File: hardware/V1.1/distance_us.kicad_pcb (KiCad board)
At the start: 2 copper layers, 20 x 45 mm, 26 parts, among them P1 CON-SENSOR, P2 CONN_4, Q1 2N7002P, Q2 2N7002P, U1 LMV358LI, U2 M24C64, U3 DRILL, U4 DRILL, U5 DRILL, U6 DRILL

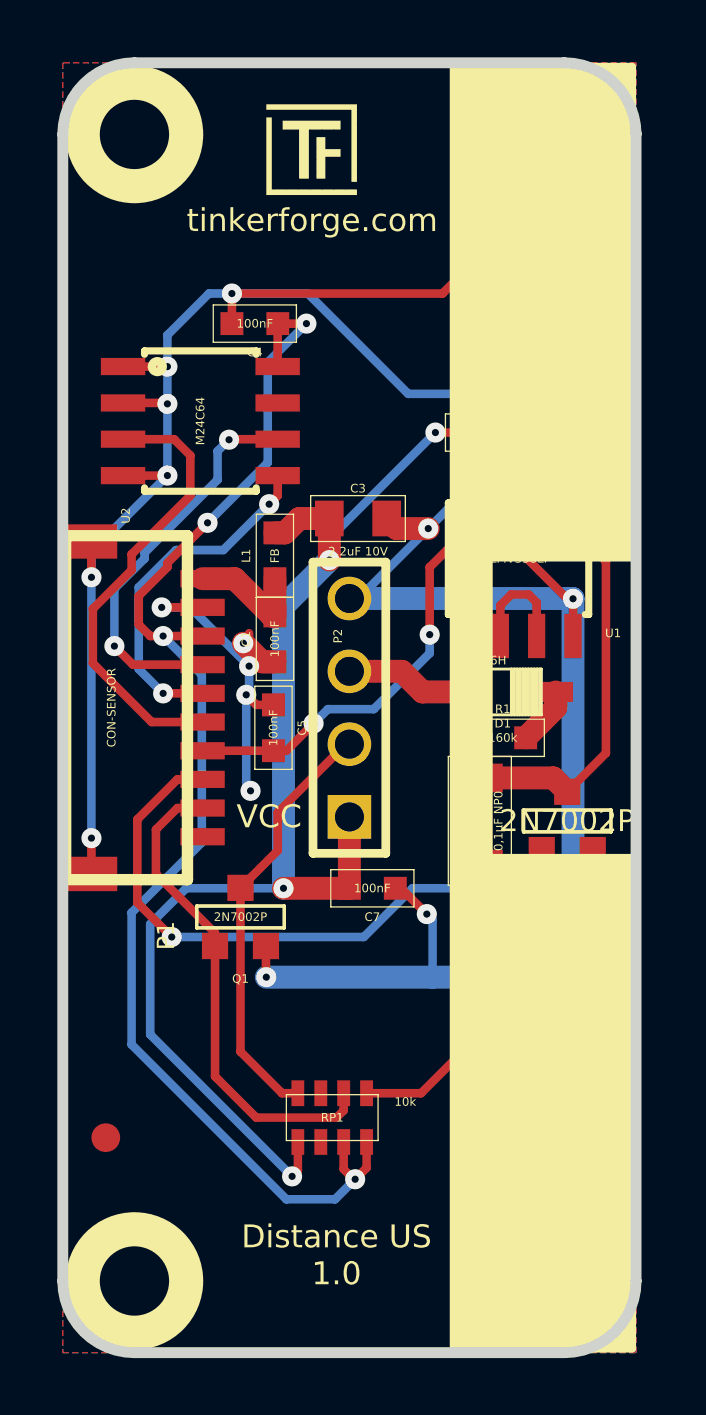
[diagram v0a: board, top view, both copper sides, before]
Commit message: new prototype to remove 5V stability problems
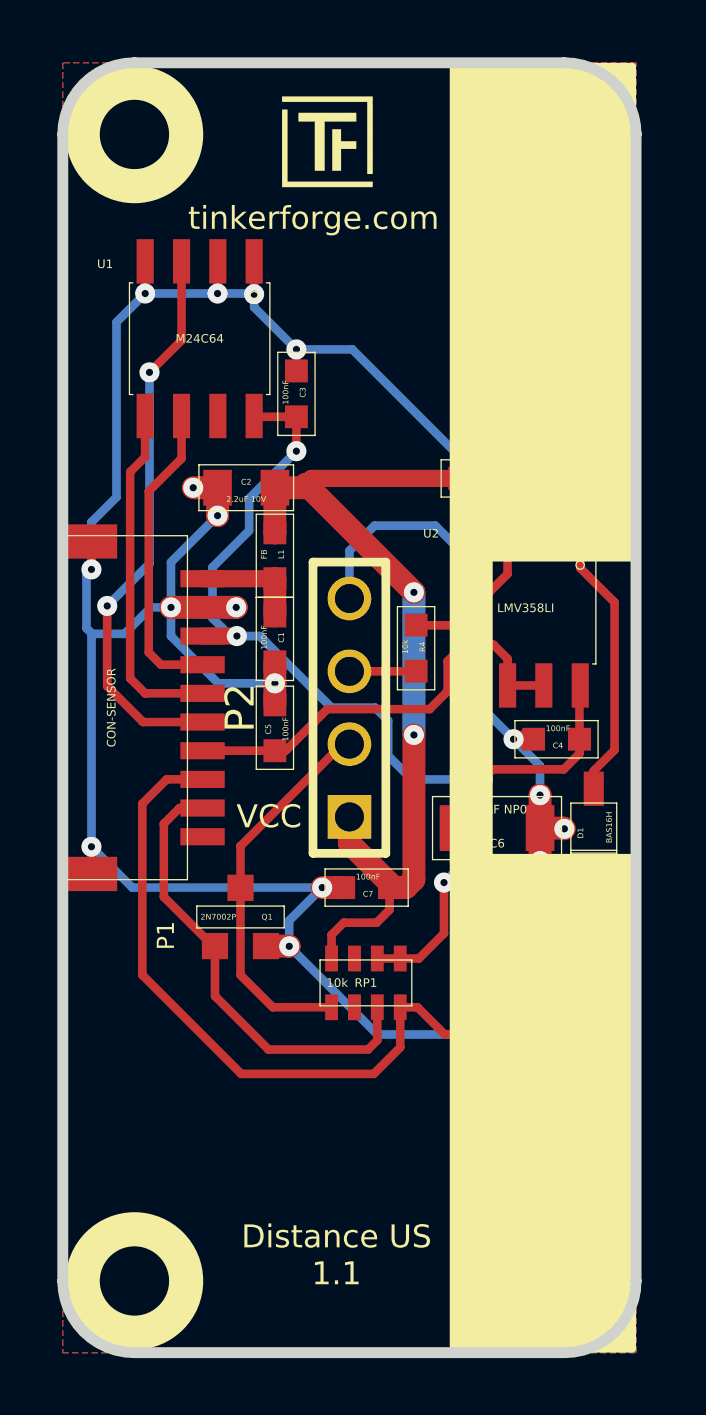
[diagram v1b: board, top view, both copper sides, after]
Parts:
- removed Fiducial_Mark (x2): VAL**, Fiducial_Mark
- removed the G*** at (50.0, 21.2)
- removed the VAL at (52.9, 50.9)
- removed the VAL at (52.9, 34.8)
- added G***: Logo_31x31, kicad-libraries:Logo_31x31, F.Cu at (50.5, 21.0)
- added R2: 10k, kicad-libraries:0603, F.Cu at (57.5, 34.3)
- added R3: 10k, kicad-libraries:0603, F.Cu at (60.5, 34.3)
- added R4: 10k, kicad-libraries:0603, F.Cu at (55.2, 40.2)
- added VAL: WEEE_7mm_back, kicad-libraries:WEEE_7mm_back, B.Cu at (52.9, 52.3)
- added VAL: CE_5mm, kicad-libraries:CE_5mm, B.Cu at (53.0, 30.5)
- C1, C4, C5, C7, L1, R1: footprint 0603 -> kicad-libraries:0603
- C2: value 100nF -> 2.2uF 10V; footprint 0603 -> kicad-libraries:0805
- C3: value 2.2uF 10V -> 100nF; footprint 0805 -> kicad-libraries:0603
- C6: footprint 1206 -> kicad-libraries:1206
- D1: footprint SOD-123 -> kicad-libraries:SOD-123
- P1: footprint CON-SENSOR -> kicad-libraries:CON-SENSOR
- P2: footprint pin_array_4x1 -> kicad-libraries:pin_array_4x1
- Q1, Q2: footprint SOT23GDS -> kicad-libraries:SOT23GDS
- RP1: footprint 0603X4 -> kicad-libraries:0603X4
- U1: value LMV358LI -> M24C64; footprint SOIC8 -> kicad-libraries:SOIC8
- U2: value M24C64 -> LMV358LI; footprint SOIC8 -> kicad-libraries:SOIC8
- U3, U4, U5, U6: footprint DRILL_NP -> kicad-libraries:DRILL_NP
- moved C4 17.9 mm to (60.1, 43.4), turned to 0 degrees
- moved U1 13.5 mm to (47.7, 29.4), turned to 180 degrees
- moved U2 13.1 mm to (59.0, 38.8), turned to 180 degrees
- moved C2 8.62 mm to (49.3, 34.6)
- moved Q2 6.83 mm to (58.2, 52.7)
- moved D1 6.11 mm to (61.4, 47.0), turned to 270 degrees
- moved R1 5.50 mm to (58.8, 48.8)
- moved C3 4.85 mm to (51.0, 31.4), turned to 90 degrees
- moved RP1 4.84 mm to (53.5, 51.9), turned to 180 degrees
- moved C6 0.65 mm to (58.0, 46.5), turned to 0 degrees
- moved C7 0.20 mm to (53.5, 48.6), turned to 0 degrees
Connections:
- C2 pad 1: GND -> VAA
- C2 pad 2: VAA -> GND
- C3 pad 1: VAA -> VCC
- C4 pad 1: VCC -> GND
- C4 pad 2: GND -> VCC
- C5 pad 2: N-0000012 -> Net-(C5-Pad2)
- C6 pad 1: N-000002 -> Net-(C6-Pad1)
- D1 pad 1: N-0000010 -> Net-(D1-Pad1)
- P1 pad 4: N-0000015 -> Net-(P1-Pad4)
- P1 pad 5: N-0000016 -> Net-(P1-Pad5)
- P1 pad 6: N-0000017 -> Net-(P1-Pad6)
- P1 pad 7: N-0000012 -> Net-(C5-Pad2)
- P1 pad 8: N-000006 -> Net-(P1-Pad8)
- P1 pad 9: N-000009 -> Net-(P1-Pad9)
- P2 pad 3: N-0000010 -> Net-(P2-Pad3)
- Q1 pad G: N-000009 -> Net-(P1-Pad9)
- Q2 pad D: N-000002 -> Net-(C6-Pad1)
- Q2 pad G: N-000006 -> Net-(P1-Pad8)
- R1 pad 1: N-000002 -> Net-(C6-Pad1)
- RP1 pad 1: N-000006 -> Trigger
- RP1 pad 2: N-000009 -> (no net)
- RP1 pad 3: (no net) -> Net-(P1-Pad9)
- RP1 pad 4: Trigger -> Net-(P1-Pad8)
- RP1 pad 5: VAA -> VCC
- RP1 pad 6: (no net) -> VCC
- RP1 pad 7: VCC -> (no net)
- RP1 pad 8: VCC -> VAA
- U1 pad 1: (no net) -> GND
- U1 pad 2: N-0000014 -> GND
- U1 pad 3: N-0000014 -> Net-(P1-Pad6)
- U1 pad 5: N-000002 -> Net-(P1-Pad5)
- U1 pad 6: N-0000012 -> Net-(P1-Pad4)
- U1 pad 7: N-0000012 -> (no net)
- U1 pad 8: VAA -> VCC
- U2 pad 1: GND -> Net-(D1-Pad1)
- U2 pad 2: GND -> Net-(R2-Pad1)
- U2 pad 3: N-0000017 -> Net-(R4-Pad2)
- U2 pad 5: N-0000016 -> Net-(C6-Pad1)
- U2 pad 6: N-0000015 -> Net-(C5-Pad2)
- U2 pad 7: (no net) -> Net-(C5-Pad2)
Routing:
- net N-000006: track 33.2 -> 0.00 mm, vias 2 -> 0
- net Net-(P1-Pad8): track 0.00 -> 23.6 mm
- net GND: track 139.8 -> 118.2 mm, vias 23 -> 20
- net Net-(P1-Pad6): track 0.00 -> 19.7 mm, vias 0 -> 2
- net N-0000012: track 19.6 -> 0.00 mm, vias 2 -> 0
- net N-000009: track 17.2 -> 0.00 mm
- net N-000002: track 16.5 -> 0.00 mm
- net Net-(P1-Pad9): track 0.00 -> 16.1 mm
- net N-0000017: track 15.9 -> 0.00 mm
- net Net-(C5-Pad2): track 0.00 -> 15.2 mm
- net VAA: track 46.4 -> 32.4 mm, vias 4 -> 2
- net N-0000015: track 13.9 -> 0.00 mm, vias 2 -> 0
- net N-0000016: track 12.3 -> 0.00 mm, vias 2 -> 0
- net Net-(P1-Pad5): track 0.00 -> 12.1 mm
- net Net-(C6-Pad1): track 0.00 -> 11.2 mm
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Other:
- board text added: "Copyright Tinkerforge GmbH 2015. This documentation describes Open Hardware and is licensed under the CERN OHL v. 1.1. You may redistribute and modify this documentation under the terms of the CERN OHL v.1.1. (http://ohwr.org/cernohl). This documentation is distributed WITHOUT ANY EXPRESS OR IMPLIED WARRANTY, INCLUDING OF MERCHANTABILITY, SATISFACTORY QUALITY AND FITNESS FOR A PARTICULAR PURPOSE.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"
- board text added: "Distance US 1.1"
- board text removed: "Copyright Tinkerforge GmbH 2013. This documentation describes Open Hardware and is licensed under the CERN OHL v. 1.1. You may redistribute and modify this documentation under the terms of the CERN OHL v.1.1. (http://ohwr.org/cernohl). This documentation is distributed WITHOUT ANY EXPRESS OR IMPLIED WARRANTY, INCLUDING OF MERCHANTABILITY, SATISFACTORY QUALITY AND FITNESS FOR A PARTICULAR PURPOSE.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"
- board text removed: "Distance US 1.0"

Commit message: fiducials added, drc run
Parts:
- added Fiducial_Mark: VAL**, kicad-libraries:Fiducial_Mark, F.Cu at (55.1, 21.3)
- added Fiducial_Mark: VAL**, kicad-libraries:Fiducial_Mark, F.Cu at (45.4, 57.3)
